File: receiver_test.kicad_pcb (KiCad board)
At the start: 2 copper layers, 70 x 65 mm, 131 parts, among them J1 RF_IN, J2 IF_IN, J3 Conn_01x02_Male, J4 Conn_01x02_Male, J6 5V, Q1 MMBT5089, Q2 BC847BS, U1 ADE-1H+, U2 SA612, U3 MCP6D11, U4 FST3253, Y1 28.636 MHz

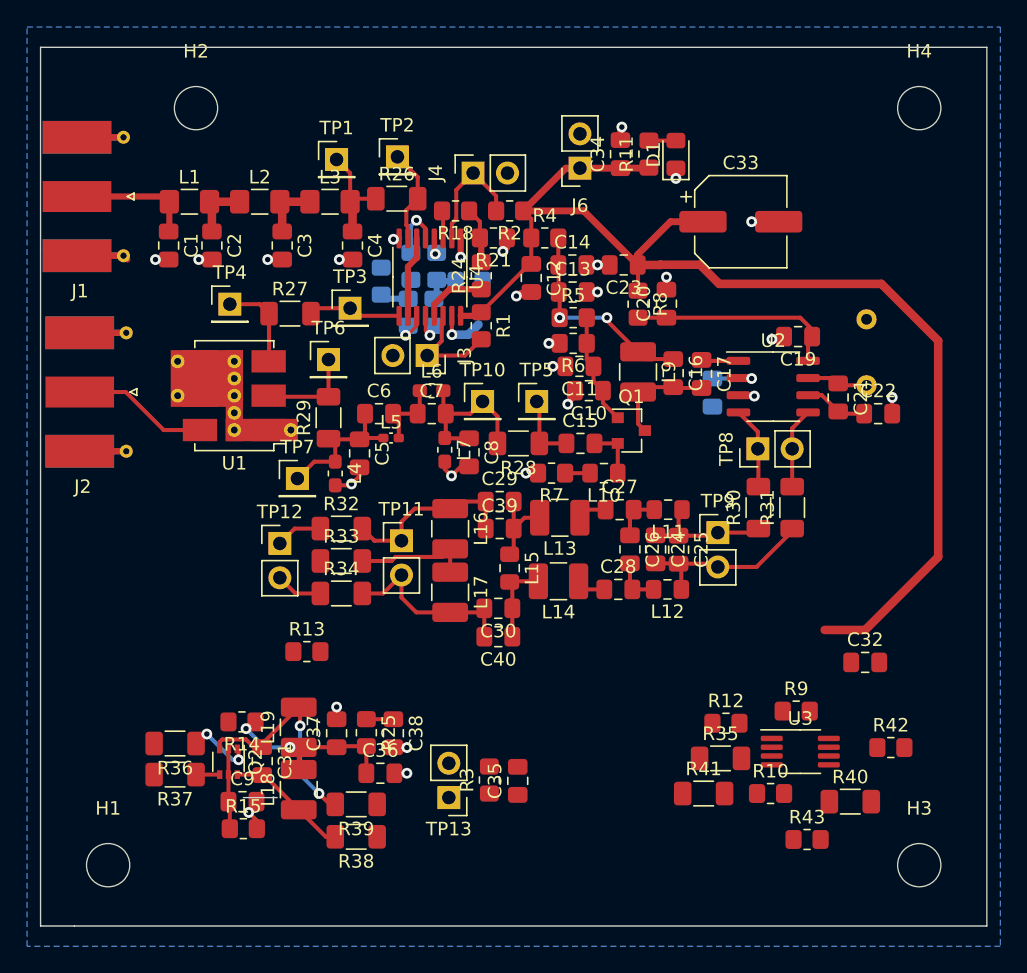
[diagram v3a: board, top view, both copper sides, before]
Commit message: Pcb edges and spacer part number
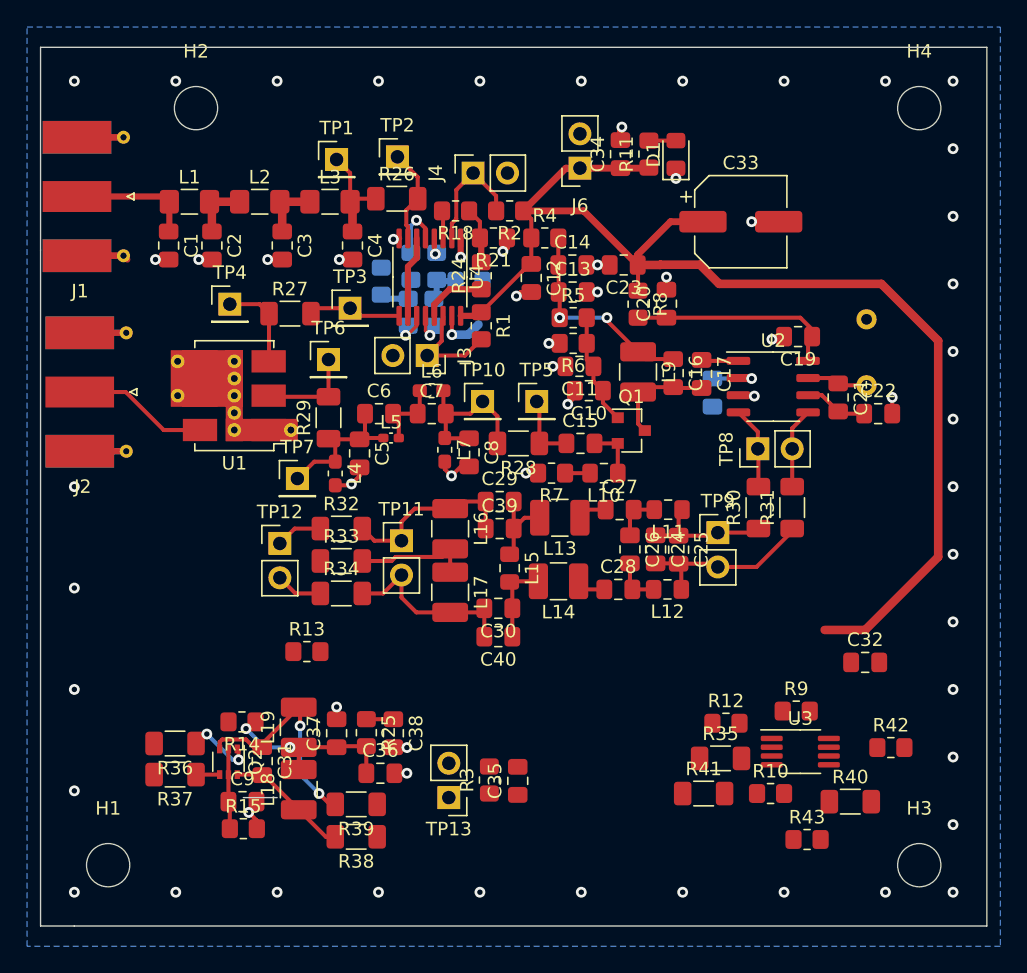
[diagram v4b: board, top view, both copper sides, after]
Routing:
- net GNDA: vias 28 -> 63
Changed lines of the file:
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@@
   (general
     (thickness 1.6)
-    (drawings 7)
-    (tracks 402)
+    (drawings 13)
+    (tracks 437)
     (zones 0)
     (modules 131)
@@
     (36 B.SilkS user)
     (37 F.SilkS user)
-    (38 B.Mask user hide)
-    (39 F.Mask user hide)
-    (40 Dwgs.User user hide)
+    (38 B.Mask user)
+    (39 F.Mask user)
+    (40 Dwgs.User user)
     (41 Cmts.User user hide)
     (42 Eco1.User user)
@@
     )
   )
+  (gr_poly (pts (xy 97.5 140) (xy 42.5 140) (xy 42.5 132.5) (xy 97.5 132.5)) (layer F.Mask) (width 0.1))
+  (gr_poly (pts (xy 97.5 140) (xy 42.5 140) (xy 42.5 132.5) (xy 97.5 132.5)) (layer B.Mask) (width 0.1))
+  (gr_poly (pts (xy 110 130) (xy 100 130) (xy 100 117.5) (xy 110 117.5)) (layer B.Mask) (width 0.1))
+  (gr_poly (pts (xy 110 130) (xy 100 130) (xy 100 117.5) (xy 110 117.5)) (layer F.Mask) (width 0.1))
+  (gr_poly (pts (xy 42.5 117.5) (xy 32.5 117.5) (xy 32.5 105) (xy 42.5 105)) (layer B.Mask) (width 0.1))
+  (gr_poly (pts (xy 42.5 117.5) (xy 32.5 117.5) (xy 32.5 105) (xy 42.5 105)) (layer F.Mask) (width 0.1))
   (gr_line (start 37.5 137.5) (end 35 137.5) (layer Edge.Cuts) (width 0.1))
   (gr_line (start 35 137.5) (end 35 87.5) (layer Edge.Cuts) (width 0.1))
@@
   (segment (start 65.431898 93.754972) (end 66.645028 93.754972) (width 0.635) (layer B.Cu) (net 1))
   (segment (start 66.645028 93.754972) (end 67.4 93) (width 0.635) (layer B.Cu) (net 1))
+  (via (at 102.5 80) (size 0.8) (drill 0.4) (layers F.Cu B.Cu) (net 1))
+  (via (at 102.5 85) (size 0.8) (drill 0.4) (layers F.Cu B.Cu) (net 1))
+  (via (at 102.5 90) (size 0.8) (drill 0.4) (layers F.Cu B.Cu) (net 1))
+  (via (at 102.5 95) (size 0.8) (drill 0.4) (layers F.Cu B.Cu) (net 1))
+  (via (at 102.5 100) (size 0.8) (drill 0.4) (layers F.Cu B.Cu) (net 1))
+  (via (at 102.5 105) (size 0.8) (drill 0.4) (layers F.Cu B.Cu) (net 1))
+  (via (at 102.5 110) (size 0.8) (drill 0.4) (layers F.Cu B.Cu) (net 1))
+  (via (at 102.5 115) (size 0.8) (drill 0.4) (layers F.Cu B.Cu) (net 1))
+  (via (at 102.5 120) (size 0.8) (drill 0.4) (layers F.Cu B.Cu) (net 1))
+  (via (at 102.5 125) (size 0.8) (drill 0.4) (layers F.Cu B.Cu) (net 1))
+  (via (at 102.5 130) (size 0.8) (drill 0.4) (layers F.Cu B.Cu) (net 1))
+  (via (at 102.5 135) (size 0.8) (drill 0.4) (layers F.Cu B.Cu) (net 1))
+  (via (at 97.5 135) (size 0.8) (drill 0.4) (layers F.Cu B.Cu) (net 1))
+  (via (at 90 135) (size 0.8) (drill 0.4) (layers F.Cu B.Cu) (net 1))
+  (via (at 82.5 135) (size 0.8) (drill 0.4) (layers F.Cu B.Cu) (net 1))
+  (via (at 75 135) (size 0.8) (drill 0.4) (layers F.Cu B.Cu) (net 1))
+  (via (at 67.5 135) (size 0.8) (drill 0.4) (layers F.Cu B.Cu) (net 1))
+  (via (at 60 135) (size 0.8) (drill 0.4) (layers F.Cu B.Cu) (net 1))
+  (via (at 52.5 135) (size 0.8) (drill 0.4) (layers F.Cu B.Cu) (net 1))
+  (via (at 45 135) (size 0.8) (drill 0.4) (layers F.Cu B.Cu) (net 1))
+  (via (at 37.5 135) (size 0.8) (drill 0.4) (layers F.Cu B.Cu) (net 1))
+  (via (at 37.5 127.5) (size 0.8) (drill 0.4) (layers F.Cu B.Cu) (net 1))
+  (via (at 37.5 120) (size 0.8) (drill 0.4) (layers F.Cu B.Cu) (net 1))
+  (via (at 37.5 112.5) (size 0.8) (drill 0.4) (layers F.Cu B.Cu) (net 1))
+  (via (at 37.5 105) (size 0.8) (drill 0.4) (layers F.Cu B.Cu) (net 1))
+  (via (at 37.5 75) (size 0.8) (drill 0.4) (layers F.Cu B.Cu) (net 1))
+  (via (at 45 75) (size 0.8) (drill 0.4) (layers F.Cu B.Cu) (net 1))
+  (via (at 52.5 75) (size 0.8) (drill 0.4) (layers F.Cu B.Cu) (net 1))
+  (via (at 60 75) (size 0.8) (drill 0.4) (layers F.Cu B.Cu) (net 1))
+  (via (at 67.5 75) (size 0.8) (drill 0.4) (layers F.Cu B.Cu) (net 1))
+  (via (at 75 75) (size 0.8) (drill 0.4) (layers F.Cu B.Cu) (net 1))
+  (via (at 82.5 75) (size 0.8) (drill 0.4) (layers F.Cu B.Cu) (net 1))
+  (via (at 90 75) (size 0.8) (drill 0.4) (layers F.Cu B.Cu) (net 1))
+  (via (at 97.5 75) (size 0.8) (drill 0.4) (layers F.Cu B.Cu) (net 1))
+  (via (at 102.5 75) (size 0.8) (drill 0.4) (layers F.Cu B.Cu) (net 1))
   (segment (start 44.138 83.536) (end 44.526 83.924) (width 0.4572) (layer F.Cu) (net 2))
   (segment (start 37.696 83.536) (end 44.138 83.536) (width 0.4572) (layer F.Cu) (net 2))

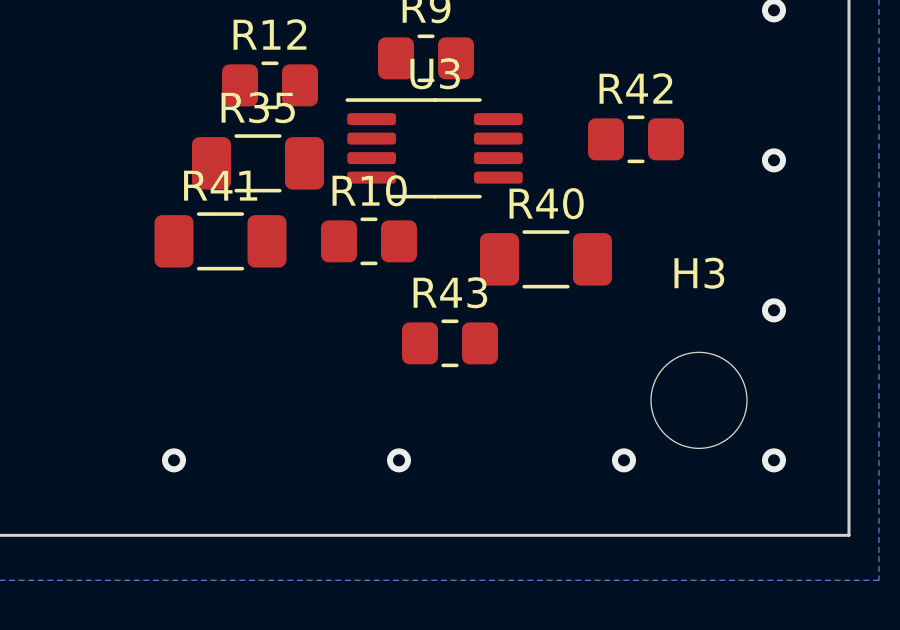
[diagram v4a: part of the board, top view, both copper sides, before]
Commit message: diffamp common mode fix
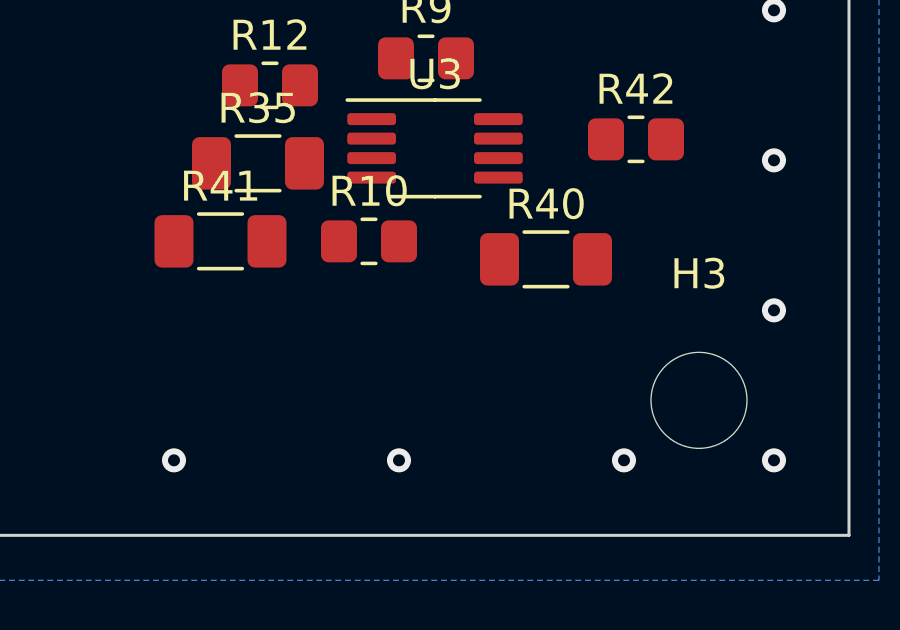
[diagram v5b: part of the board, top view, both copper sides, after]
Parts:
- removed R43: 19k, Resistor_SMD:R_0805_2012Metric_Pad1.20x1.40mm_HandSolder
- R42: value 19k -> BP
- Y1: value 28.636 MHz -> 28.224 MHz
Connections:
- net /37.4 MHz BPF/IN renamed /37.224 MHz BPF/IN
- C32 pad 1: /Sheet5FE3342E/DC_CM -> Net-(C32-Pad1)
- C7 pad 2: /37.4 MHz BPF/OUT -> /37.224 MHz BPF/OUT
- C8 pad 1: /37.4 MHz BPF/OUT -> /37.224 MHz BPF/OUT
- L6 pad 2: /37.4 MHz BPF/OUT -> /37.224 MHz BPF/OUT
- L7 pad 1: /37.4 MHz BPF/OUT -> /37.224 MHz BPF/OUT
- R28 pad 2: /37.4 MHz BPF/OUT -> Net-(R28-Pad2)
- R42 pad 1: +5VA -> Net-(C32-Pad1)
- TP10 pad 1: /37.4 MHz BPF/OUT -> Net-(R28-Pad2)
- U3 pad 2: /Sheet5FE3342E/DC_CM -> Net-(C32-Pad1)

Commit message: PCB is Done... Needs DRC check
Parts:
- removed the R12 at (85.7, 122.5)
- added R9: BP, Resistor_SMD:R_1206_3216Metric_Pad1.42x1.75mm_HandSolder, F.Cu at (76.9, 122.7)
- moved R16 20.8 mm to (77.5, 120.4), turned to 180 degrees
- moved R14 20.6 mm to (74.3, 128.3)
- moved C32 16.8 mm to (80.5, 124.5), turned to 270 degrees
- moved R10 11.0 mm to (76.8, 118.1), turned to 180 degrees
- moved R15 9.98 mm to (74.3, 125.5)
- moved U3 8.60 mm to (83.6, 120.7)
- moved R12 8.11 mm to (83.7, 117.9)
- moved R13 5.97 mm to (84.7, 123.6), turned to 180 degrees
- renumbered C11 to C10, C12 to C11, C13 to C12, C14 to C13, C15 to C14, C16 to C15, C17 to C16, C18 to C17, C19 to C18, C20 to C19, C21 to C20, C22 to C21, C23 to C22, C24 to C23, C25 to C24, C26 to C25, C27 to C26, C28 to C27, C39 to C28, C40 to C31, C9 to C39, C31 to C40, C10 to C9, L11 to L10, L12 to L11, L13 to L12, L14 to L13, L15 to L14, L16 to L15, L17 to L16, L18 to L17, L19 to L18, L9 to L8, L10 to L9, R35 to R10, R9 to R12, R10 to R13, R40 to R14, R41 to R15, R42 to R16, R36 to R17, R37 to R18, R13 to R19, R38 to R20, R39 to R21, R14 to R22, R15 to R23, R16 to R24, R17 to R35, R18 to R36, R19 to R37, R20 to R38, R21 to R39, R22 to R40, R23 to R41, R24 to R42
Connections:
- C32 pad 2: GND -> GNDA
- U3 pad 6: GND -> GNDA
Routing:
- net /Sheet5FE3342E/In-: track 3.48 -> 55.8 mm
- net /Sheet5FE3342E/In+: track 3.46 -> 49.3 mm
- net +5VA: track 93.4 -> 132.1 mm, vias 0 -> 4
- net /Sheet5FE3342E/DC_CM: track 0.00 -> 29.8 mm
- net Net-(R12-Pad1): track 0.00 -> 22.3 mm
- net Net-(R13-Pad1): track 0.00 -> 20.6 mm
- net Net-(R12-Pad2): track 0.00 -> 16.9 mm
- net /Sheet5FE3342E/Out+: track 0.00 -> 15.2 mm
- net /Sheet5FE3342E/Out-: track 0.00 -> 14.1 mm
- net Net-(R10-Pad1): track 0.00 -> 9.14 mm
- net Net-(C32-Pad1): track 0.00 -> 6.91 mm
- net GNDA: track 44.5 -> 47.9 mm, vias 63 -> 66

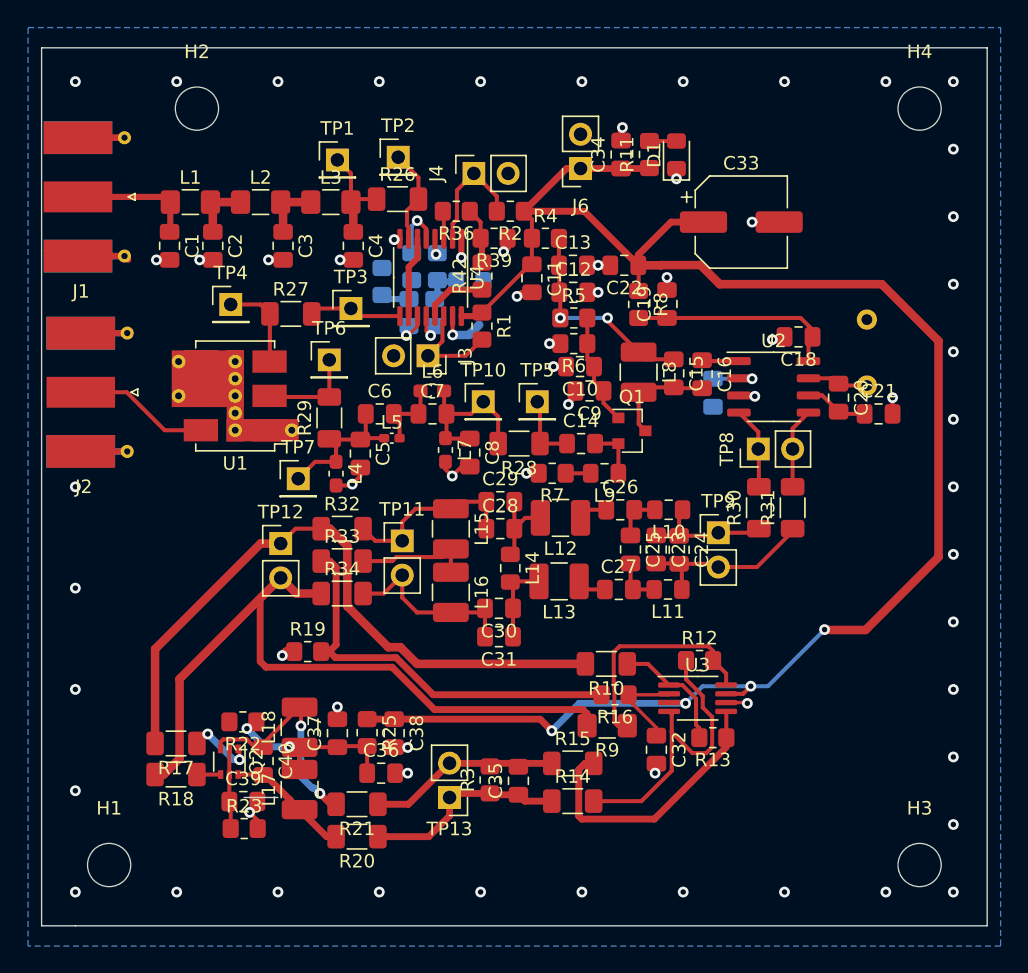
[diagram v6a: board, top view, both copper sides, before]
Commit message: RX PCB revision: Diff amp + Mixer2
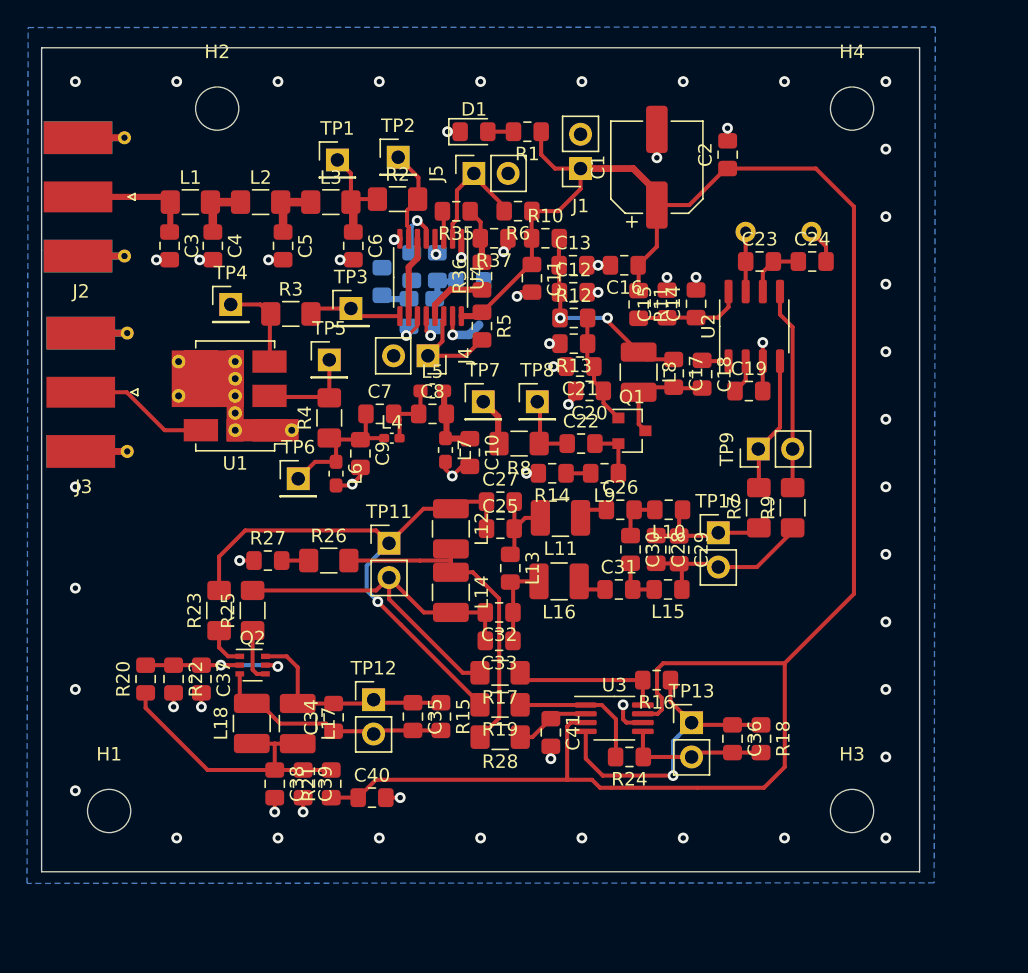
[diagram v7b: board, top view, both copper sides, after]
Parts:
- removed the R14 at (74.3, 128.3)
- removed the R20 at (58.4, 130.9)
- removed the R21 at (58.4, 128.5)
- removed the R3 at (68.2, 126.7)
- removed the R32 at (57.2, 108.1)
- removed the R33 at (57.2, 110.5)
- removed the R34 at (57.2, 112.9)
- removed the TP11 at (61.7, 109.0)
- added C36: 10p, Capacitor_SMD:C_0805_2012Metric_Pad1.15x1.40mm_HandSolder, F.Cu at (86.2, 123.7)
- added R18: 10k, Resistor_SMD:R_0805_2012Metric_Pad1.15x1.40mm_HandSolder, F.Cu at (88.3, 123.7)
- added R26: BP, Resistor_SMD:R_1206_3216Metric_Pad1.42x1.75mm_HandSolder, F.Cu at (56.3, 110.5)
- added TP12: TestPoint_2Pole, Connector_PinHeader_2.54mm:PinHeader_1x02_P2.54mm_Vertical, F.Cu at (59.6, 120.8)
- C10: renamed from C8; footprint Capacitor_SMD:C_0805_2012Metric_Pad1.18x1.45mm_HandSolder -> Capacitor_SMD:C_0805_2012Metric_Pad1.15x1.40mm_HandSolder
- C11, C12, C13, C26, C35: footprint Capacitor_SMD:C_0805_2012Metric_Pad1.18x1.45mm_HandSolder -> Capacitor_SMD:C_0805_2012Metric_Pad1.15x1.40mm_HandSolder
- C14: renamed from C18; footprint Capacitor_SMD:C_0805_2012Metric_Pad1.18x1.45mm_HandSolder -> Capacitor_SMD:C_0805_2012Metric_Pad1.15x1.40mm_HandSolder
- C15: renamed from C19; footprint Capacitor_SMD:C_0805_2012Metric_Pad1.18x1.45mm_HandSolder -> Capacitor_SMD:C_0805_2012Metric_Pad1.15x1.40mm_HandSolder
- C16: renamed from C22; footprint Capacitor_SMD:C_0805_2012Metric_Pad1.18x1.45mm_HandSolder -> Capacitor_SMD:C_0805_2012Metric_Pad1.15x1.40mm_HandSolder
- C17: renamed from C15; footprint Capacitor_SMD:C_0805_2012Metric_Pad1.18x1.45mm_HandSolder -> Capacitor_SMD:C_0805_2012Metric_Pad1.15x1.40mm_HandSolder
- C18: renamed from C16; footprint Capacitor_SMD:C_0805_2012Metric_Pad1.18x1.45mm_HandSolder -> Capacitor_SMD:C_0805_2012Metric_Pad1.15x1.40mm_HandSolder
- C19: renamed from C17; footprint Capacitor_SMD:C_0805_2012Metric_Pad1.18x1.45mm_HandSolder -> Capacitor_SMD:C_0805_2012Metric_Pad1.15x1.40mm_HandSolder; moved to F.Cu
- C2: renamed from C34; footprint Capacitor_SMD:C_0805_2012Metric_Pad1.18x1.45mm_HandSolder -> Capacitor_SMD:C_0805_2012Metric_Pad1.15x1.40mm_HandSolder
- C20: renamed from C9; footprint Capacitor_SMD:C_0805_2012Metric_Pad1.18x1.45mm_HandSolder -> Capacitor_SMD:C_0805_2012Metric_Pad1.15x1.40mm_HandSolder
- C21: renamed from C10; footprint Capacitor_SMD:C_0805_2012Metric_Pad1.18x1.45mm_HandSolder -> Capacitor_SMD:C_0805_2012Metric_Pad1.15x1.40mm_HandSolder
- C22: renamed from C14; footprint Capacitor_SMD:C_0805_2012Metric_Pad1.18x1.45mm_HandSolder -> Capacitor_SMD:C_0805_2012Metric_Pad1.15x1.40mm_HandSolder
- C23: renamed from C20; footprint Capacitor_SMD:C_0805_2012Metric_Pad1.18x1.45mm_HandSolder -> Capacitor_SMD:C_0805_2012Metric_Pad1.15x1.40mm_HandSolder
- C24: renamed from C21; footprint Capacitor_SMD:C_0805_2012Metric_Pad1.18x1.45mm_HandSolder -> Capacitor_SMD:C_0805_2012Metric_Pad1.15x1.40mm_HandSolder
- C25: renamed from C28; footprint Capacitor_SMD:C_0805_2012Metric_Pad1.18x1.45mm_HandSolder -> Capacitor_SMD:C_0805_2012Metric_Pad1.15x1.40mm_HandSolder
- C27: renamed from C29; footprint Capacitor_SMD:C_0805_2012Metric_Pad1.18x1.45mm_HandSolder -> Capacitor_SMD:C_0805_2012Metric_Pad1.15x1.40mm_HandSolder
- C28: renamed from C23; footprint Capacitor_SMD:C_0805_2012Metric_Pad1.18x1.45mm_HandSolder -> Capacitor_SMD:C_0805_2012Metric_Pad1.15x1.40mm_HandSolder
- C29: renamed from C24; footprint Capacitor_SMD:C_0805_2012Metric_Pad1.18x1.45mm_HandSolder -> Capacitor_SMD:C_0805_2012Metric_Pad1.15x1.40mm_HandSolder
- C3: renamed from C1; footprint Capacitor_SMD:C_0805_2012Metric_Pad1.18x1.45mm_HandSolder -> Capacitor_SMD:C_0805_2012Metric_Pad1.15x1.40mm_HandSolder
- C30: renamed from C25; footprint Capacitor_SMD:C_0805_2012Metric_Pad1.18x1.45mm_HandSolder -> Capacitor_SMD:C_0805_2012Metric_Pad1.15x1.40mm_HandSolder
- C31: renamed from C27; footprint Capacitor_SMD:C_0805_2012Metric_Pad1.18x1.45mm_HandSolder -> Capacitor_SMD:C_0805_2012Metric_Pad1.15x1.40mm_HandSolder
- C32: renamed from C30; footprint Capacitor_SMD:C_0805_2012Metric_Pad1.18x1.45mm_HandSolder -> Capacitor_SMD:C_0805_2012Metric_Pad1.15x1.40mm_HandSolder
- C33: renamed from C31; footprint Capacitor_SMD:C_0805_2012Metric_Pad1.18x1.45mm_HandSolder -> Capacitor_SMD:C_0805_2012Metric_Pad1.15x1.40mm_HandSolder
- C34: renamed from C40; footprint Capacitor_SMD:C_0805_2012Metric_Pad1.18x1.45mm_HandSolder -> Capacitor_SMD:C_0805_2012Metric_Pad1.15x1.40mm_HandSolder
- C37: renamed from C39; footprint Capacitor_SMD:C_0805_2012Metric_Pad1.18x1.45mm_HandSolder -> Capacitor_SMD:C_0805_2012Metric_Pad1.15x1.40mm_HandSolder
- C38: renamed from C36; footprint Capacitor_SMD:C_0805_2012Metric_Pad1.18x1.45mm_HandSolder -> Capacitor_SMD:C_0805_2012Metric_Pad1.15x1.40mm_HandSolder
- C39: renamed from C37; footprint Capacitor_SMD:C_0805_2012Metric_Pad1.18x1.45mm_HandSolder -> Capacitor_SMD:C_0805_2012Metric_Pad1.15x1.40mm_HandSolder
- C4: renamed from C2; footprint Capacitor_SMD:C_0805_2012Metric_Pad1.18x1.45mm_HandSolder -> Capacitor_SMD:C_0805_2012Metric_Pad1.15x1.40mm_HandSolder
- C40: renamed from C38; footprint Capacitor_SMD:C_0805_2012Metric_Pad1.18x1.45mm_HandSolder -> Capacitor_SMD:C_0805_2012Metric_Pad1.15x1.40mm_HandSolder
- C41: renamed from C32; footprint Capacitor_SMD:C_0805_2012Metric_Pad1.18x1.45mm_HandSolder -> Capacitor_SMD:C_0805_2012Metric_Pad1.15x1.40mm_HandSolder
- C5: renamed from C3; footprint Capacitor_SMD:C_0805_2012Metric_Pad1.18x1.45mm_HandSolder -> Capacitor_SMD:C_0805_2012Metric_Pad1.15x1.40mm_HandSolder
- C6: renamed from C4; footprint Capacitor_SMD:C_0805_2012Metric_Pad1.18x1.45mm_HandSolder -> Capacitor_SMD:C_0805_2012Metric_Pad1.15x1.40mm_HandSolder
- C7: renamed from C6; footprint Capacitor_SMD:C_0805_2012Metric_Pad1.18x1.45mm_HandSolder -> Capacitor_SMD:C_0805_2012Metric_Pad1.15x1.40mm_HandSolder
- C8: renamed from C7; footprint Capacitor_SMD:C_0805_2012Metric_Pad1.18x1.45mm_HandSolder -> Capacitor_SMD:C_0805_2012Metric_Pad1.15x1.40mm_HandSolder
- C9: renamed from C5; footprint Capacitor_SMD:C_0805_2012Metric_Pad1.18x1.45mm_HandSolder -> Capacitor_SMD:C_0805_2012Metric_Pad1.15x1.40mm_HandSolder
- R1: renamed from R11; footprint Resistor_SMD:R_0805_2012Metric_Pad1.20x1.40mm_HandSolder -> Resistor_SMD:R_0805_2012Metric_Pad1.15x1.40mm_HandSolder
- R10: renamed from R4; footprint Resistor_SMD:R_0805_2012Metric_Pad1.20x1.40mm_HandSolder -> Resistor_SMD:R_0805_2012Metric_Pad1.15x1.40mm_HandSolder
- R11: renamed from R8; footprint Resistor_SMD:R_0805_2012Metric_Pad1.20x1.40mm_HandSolder -> Resistor_SMD:R_0805_2012Metric_Pad1.15x1.40mm_HandSolder
- R12: renamed from R5; footprint Resistor_SMD:R_0805_2012Metric_Pad1.20x1.40mm_HandSolder -> Resistor_SMD:R_0805_2012Metric_Pad1.15x1.40mm_HandSolder
- R13: renamed from R6; footprint Resistor_SMD:R_0805_2012Metric_Pad1.20x1.40mm_HandSolder -> Resistor_SMD:R_0805_2012Metric_Pad1.15x1.40mm_HandSolder
- R14: renamed from R7; footprint Resistor_SMD:R_0805_2012Metric_Pad1.20x1.40mm_HandSolder -> Resistor_SMD:R_0805_2012Metric_Pad1.15x1.40mm_HandSolder
- R15: value BP -> 10k; footprint Resistor_SMD:R_1206_3216Metric_Pad1.30x1.75mm_HandSolder -> Resistor_SMD:R_0805_2012Metric_Pad1.15x1.40mm_HandSolder
- R16: renamed from R12; footprint Resistor_SMD:R_0805_2012Metric_Pad1.20x1.40mm_HandSolder -> Resistor_SMD:R_0805_2012Metric_Pad1.15x1.40mm_HandSolder
- R19: renamed from R10; footprint Resistor_SMD:R_1206_3216Metric_Pad1.30x1.75mm_HandSolder -> Resistor_SMD:R_1206_3216Metric_Pad1.42x1.75mm_HandSolder
- R2: renamed from R26; footprint Resistor_SMD:R_1206_3216Metric_Pad1.30x1.75mm_HandSolder -> Resistor_SMD:R_1206_3216Metric_Pad1.42x1.75mm_HandSolder
- R20: renamed from R22; footprint Resistor_SMD:R_0805_2012Metric_Pad1.20x1.40mm_HandSolder -> Resistor_SMD:R_0805_2012Metric_Pad1.15x1.40mm_HandSolder
- R21: renamed from R25; footprint Resistor_SMD:R_0805_2012Metric_Pad1.20x1.40mm_HandSolder -> Resistor_SMD:R_0805_2012Metric_Pad1.15x1.40mm_HandSolder
- R22: renamed from R23; footprint Resistor_SMD:R_0805_2012Metric_Pad1.20x1.40mm_HandSolder -> Resistor_SMD:R_0805_2012Metric_Pad1.15x1.40mm_HandSolder
- R23: renamed from R17; footprint Resistor_SMD:R_1206_3216Metric_Pad1.30x1.75mm_HandSolder -> Resistor_SMD:R_1206_3216Metric_Pad1.42x1.75mm_HandSolder
- R24: renamed from R13; footprint Resistor_SMD:R_0805_2012Metric_Pad1.20x1.40mm_HandSolder -> Resistor_SMD:R_0805_2012Metric_Pad1.15x1.40mm_HandSolder
- R25: renamed from R18; footprint Resistor_SMD:R_1206_3216Metric_Pad1.30x1.75mm_HandSolder -> Resistor_SMD:R_1206_3216Metric_Pad1.42x1.75mm_HandSolder
- R27: renamed from R19; footprint Resistor_SMD:R_0805_2012Metric_Pad1.20x1.40mm_HandSolder -> Resistor_SMD:R_0805_2012Metric_Pad1.15x1.40mm_HandSolder
- R28: renamed from R16; footprint Resistor_SMD:R_0805_2012Metric_Pad1.20x1.40mm_HandSolder -> Resistor_SMD:R_1206_3216Metric_Pad1.42x1.75mm_HandSolder
- R29: renamed from R24; footprint Resistor_SMD:R_0805_2012Metric_Pad1.20x1.40mm_HandSolder -> Resistor_SMD:R_0805_2012Metric_Pad1.15x1.40mm_HandSolder
- R3: renamed from R27; footprint Resistor_SMD:R_1206_3216Metric_Pad1.30x1.75mm_HandSolder -> Resistor_SMD:R_1206_3216Metric_Pad1.42x1.75mm_HandSolder
- R30: renamed from R40; footprint Resistor_SMD:R_0805_2012Metric_Pad1.20x1.40mm_HandSolder -> Resistor_SMD:R_0805_2012Metric_Pad1.15x1.40mm_HandSolder
- R31: renamed from R37; footprint Resistor_SMD:R_0805_2012Metric_Pad1.20x1.40mm_HandSolder -> Resistor_SMD:R_0805_2012Metric_Pad1.15x1.40mm_HandSolder
- R32: renamed from R35; footprint Resistor_SMD:R_0805_2012Metric_Pad1.20x1.40mm_HandSolder -> Resistor_SMD:R_0805_2012Metric_Pad1.15x1.40mm_HandSolder
- R33: renamed from R41; footprint Resistor_SMD:R_0805_2012Metric_Pad1.20x1.40mm_HandSolder -> Resistor_SMD:R_0805_2012Metric_Pad1.15x1.40mm_HandSolder
- R34: renamed from R38; footprint Resistor_SMD:R_0805_2012Metric_Pad1.20x1.40mm_HandSolder -> Resistor_SMD:R_0805_2012Metric_Pad1.15x1.40mm_HandSolder
- R35: renamed from R36; footprint Resistor_SMD:R_0805_2012Metric_Pad1.20x1.40mm_HandSolder -> Resistor_SMD:R_0805_2012Metric_Pad1.15x1.40mm_HandSolder
- R36: renamed from R42; footprint Resistor_SMD:R_0805_2012Metric_Pad1.20x1.40mm_HandSolder -> Resistor_SMD:R_0805_2012Metric_Pad1.15x1.40mm_HandSolder
- R37: renamed from R39; footprint Resistor_SMD:R_0805_2012Metric_Pad1.20x1.40mm_HandSolder -> Resistor_SMD:R_0805_2012Metric_Pad1.15x1.40mm_HandSolder
- R4: renamed from R29; footprint Resistor_SMD:R_1206_3216Metric_Pad1.30x1.75mm_HandSolder -> Resistor_SMD:R_1206_3216Metric_Pad1.42x1.75mm_HandSolder
- R5: renamed from R1; footprint Resistor_SMD:R_0805_2012Metric_Pad1.20x1.40mm_HandSolder -> Resistor_SMD:R_0805_2012Metric_Pad1.15x1.40mm_HandSolder
- R6: renamed from R2; footprint Resistor_SMD:R_0805_2012Metric_Pad1.20x1.40mm_HandSolder -> Resistor_SMD:R_0805_2012Metric_Pad1.15x1.40mm_HandSolder
- R7: renamed from R30; footprint Resistor_SMD:R_1206_3216Metric_Pad1.30x1.75mm_HandSolder -> Resistor_SMD:R_1206_3216Metric_Pad1.42x1.75mm_HandSolder
- R8: renamed from R28; footprint Resistor_SMD:R_1206_3216Metric_Pad1.30x1.75mm_HandSolder -> Resistor_SMD:R_1206_3216Metric_Pad1.42x1.75mm_HandSolder
- R9: renamed from R31; footprint Resistor_SMD:R_1206_3216Metric_Pad1.30x1.75mm_HandSolder -> Resistor_SMD:R_1206_3216Metric_Pad1.42x1.75mm_HandSolder
- moved TP13 18.8 mm to (83.1, 122.5), turned to 0 degrees
- moved D1 15.1 mm to (67.0, 78.7), turned to 0 degrees
- moved Y1 14.5 mm to (87.1, 86.1), turned to 0 degrees
- moved R25 13.4 mm to (50.6, 114.2), turned to 90 degrees
- moved C24 12.3 mm to (92.0, 88.3)
- moved R22 12.2 mm to (44.8, 119.2), turned to 270 degrees
- moved C23 11.7 mm to (88.2, 88.3), turned to 0 degrees
- moved R15 10.4 mm to (64.6, 122.0), turned to 270 degrees
- moved R23 10.3 mm to (48.1, 114.2), turned to 90 degrees
- moved C37 9.59 mm to (46.8, 119.2), turned to 270 degrees
- moved R1 9.20 mm to (71.0, 78.7), turned to 180 degrees
- moved C35 9.14 mm to (62.5, 122.0), turned to 270 degrees
- moved R28 9.06 mm to (69.0, 123.5)
- moved R17 8.84 mm to (68.9, 118.8)
- moved R19 8.43 mm to (68.9, 121.1)
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- renumbered C33 to C1, J6 to J1, J1 to J2, J2 to J3, J3 to J4, J4 to J5, L12 to L11, L15 to L12, L14 to L13, L16 to L14, L11 to L15, L13 to L16, L5 to L4, L6 to L5, L4 to L6, R9 to R17, TP9 to TP10, TP12 to TP11, TP6 to TP5, TP7 to TP6, TP10 to TP7, TP5 to TP8, TP8 to TP9
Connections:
- C25 pad 1: /Sheet5FE333A0/Out+ -> /Sheet5FE3342E/In+
- C27 pad 1: /Sheet5FE333A0/Out+ -> /Sheet5FE3342E/In+
- C32 pad 2: /Sheet5FE333A0/Out- -> /Sheet5FE3342E/In-
- C33 pad 2: /Sheet5FE333A0/Out- -> /Sheet5FE3342E/In-
- C34 pad 1: Net-(C40-Pad1) -> Net-(C34-Pad1)
- C34 pad 2: Net-(C40-Pad2) -> Net-(C34-Pad2)
- C35 pad 1: /Sheet5FE3342E/Out+ -> Net-(C34-Pad2)
- C35 pad 2: /Sheet5FE3342E/Out- -> Net-(C34-Pad1)
- L12 pad 1: /Sheet5FE333A0/Out+ -> /Sheet5FE3342E/In+
- L14 pad 2: /Sheet5FE333A0/Out- -> /Sheet5FE3342E/In-
- L17 pad 1: Net-(C40-Pad2) -> Net-(C34-Pad2)
- L18 pad 2: Net-(C40-Pad1) -> Net-(C34-Pad1)
- Q2 pad 3: Net-(C40-Pad1) -> Net-(C34-Pad1)
- Q2 pad 6: Net-(C40-Pad2) -> Net-(C34-Pad2)
- R15 pad 1: /Sheet5FE3342E/Out- -> Net-(C34-Pad2)
- R15 pad 2: Net-(R13-Pad1) -> Net-(C34-Pad1)
- R16 pad 1: Net-(R12-Pad1) -> Net-(C36-Pad1)
- R24 pad 1: Net-(R13-Pad1) -> Net-(C36-Pad2)
- R27 pad 2: /Sheet5FE3342E/DC_CM -> Net-(R26-Pad1)
- R28 pad 2: /Sheet5FE3342E/DC_CM -> /Sheet5FE333A0/DC_CM
- TP13 pad 1: /Sheet5FE3342E/Out+ -> Net-(C36-Pad1)
- TP13 pad 2: /Sheet5FE3342E/Out- -> Net-(C36-Pad2)
- U3 pad 4: Net-(R12-Pad1) -> Net-(C36-Pad1)
- U3 pad 5: Net-(R13-Pad1) -> Net-(C36-Pad2)
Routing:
- net /Sheet5FE3342E/DC_CM: track 29.8 -> 0.00 mm
- net GNDA: track 47.9 -> 73.3 mm, vias 66 -> 62
- net /Sheet5FE3342E/In-: track 55.8 -> 32.5 mm
- net Net-(C36-Pad1): track 0.00 -> 22.5 mm, vias 0 -> 1
- net Net-(R12-Pad1): track 22.3 -> 0.00 mm
- net Net-(R13-Pad1): track 20.6 -> 0.00 mm
- net +5VA: track 132.1 -> 151.1 mm, vias 4 -> 0
- net Net-(C34-Pad1): track 0.00 -> 18.0 mm
- net Net-(C40-Pad1): track 16.7 -> 0.00 mm, vias 2 -> 0
- net Net-(C34-Pad2): track 0.00 -> 16.2 mm
- net /Sheet5FE333A0/DC_CM: track 8.60 -> 24.5 mm
- net /Sheet5FE3342E/Out+: track 15.2 -> 0.00 mm
- net /Sheet5FE3342E/Out-: track 14.1 -> 0.00 mm
- net /Sheet5FE333A0/Out-: track 13.9 -> 0.00 mm
- net /Sheet5FE333A0/Out+: track 13.5 -> 0.00 mm
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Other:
- board size 70 x 65 mm -> 65 x 61 mm
